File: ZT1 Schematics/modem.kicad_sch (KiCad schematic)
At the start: 3 parts, among them U145 74LS153, U146 74LS153

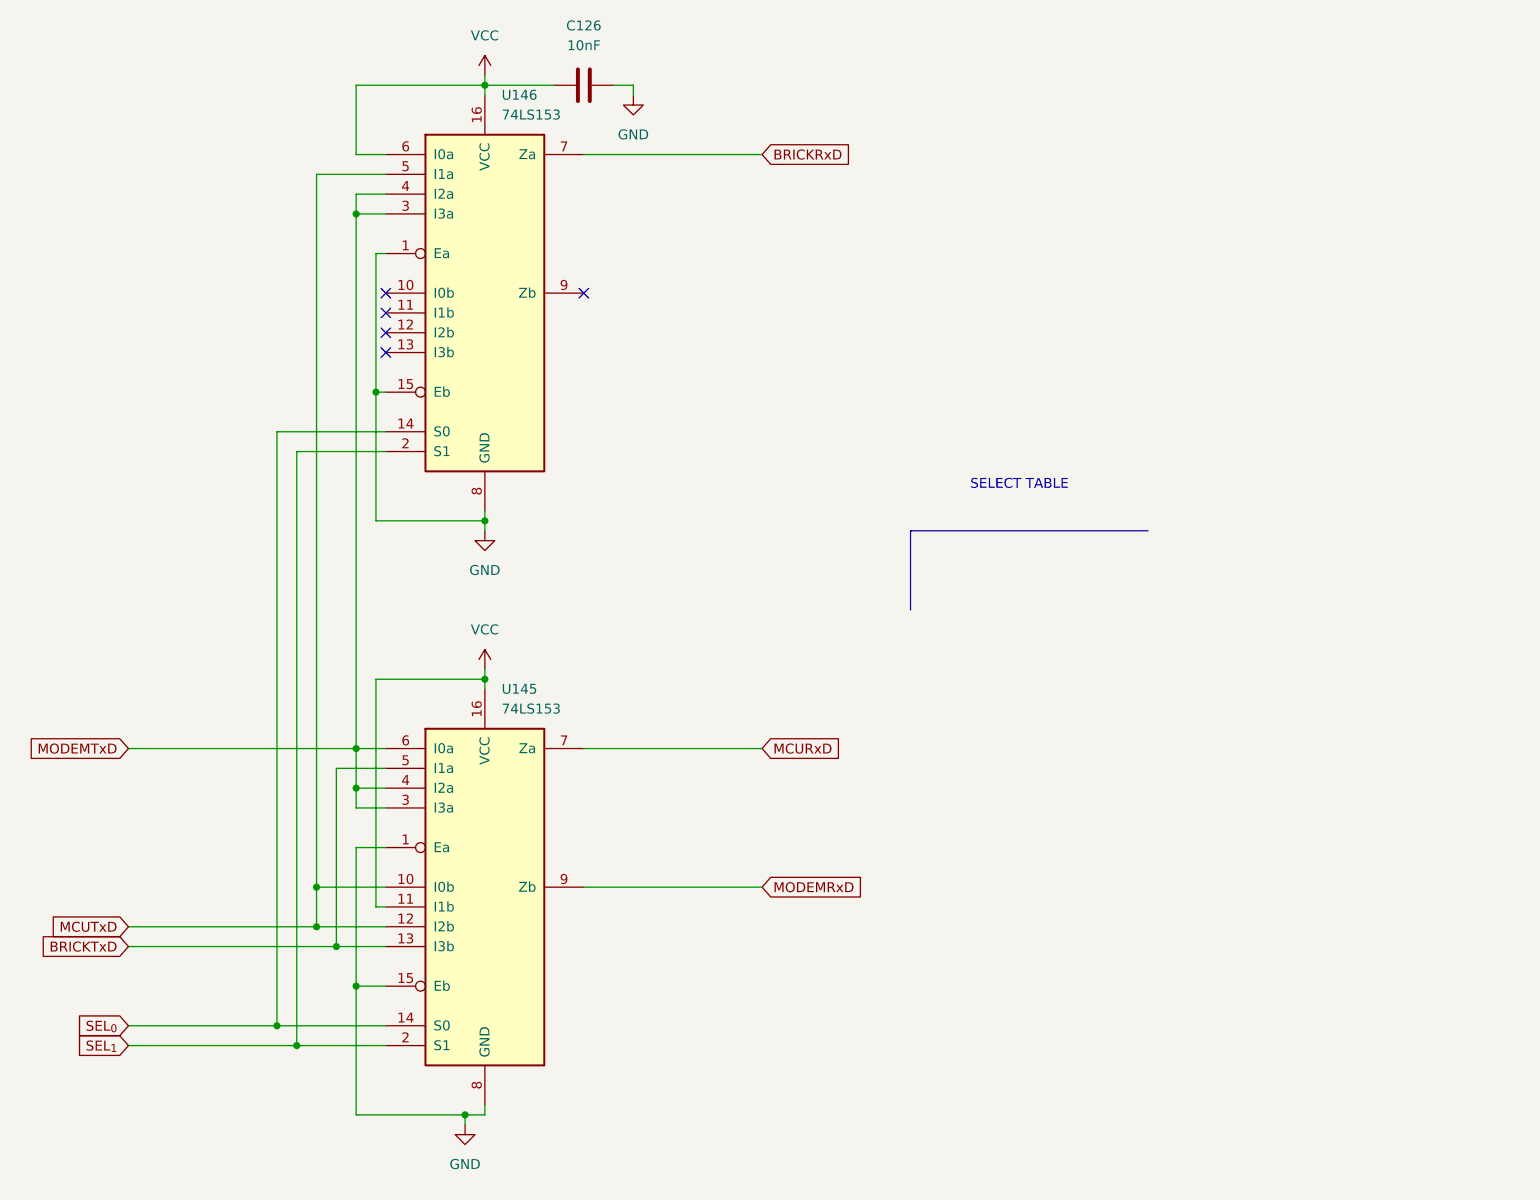
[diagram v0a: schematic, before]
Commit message: Minor touchups
Fixed some of the text
Added some explanations
Simplified the video circuit
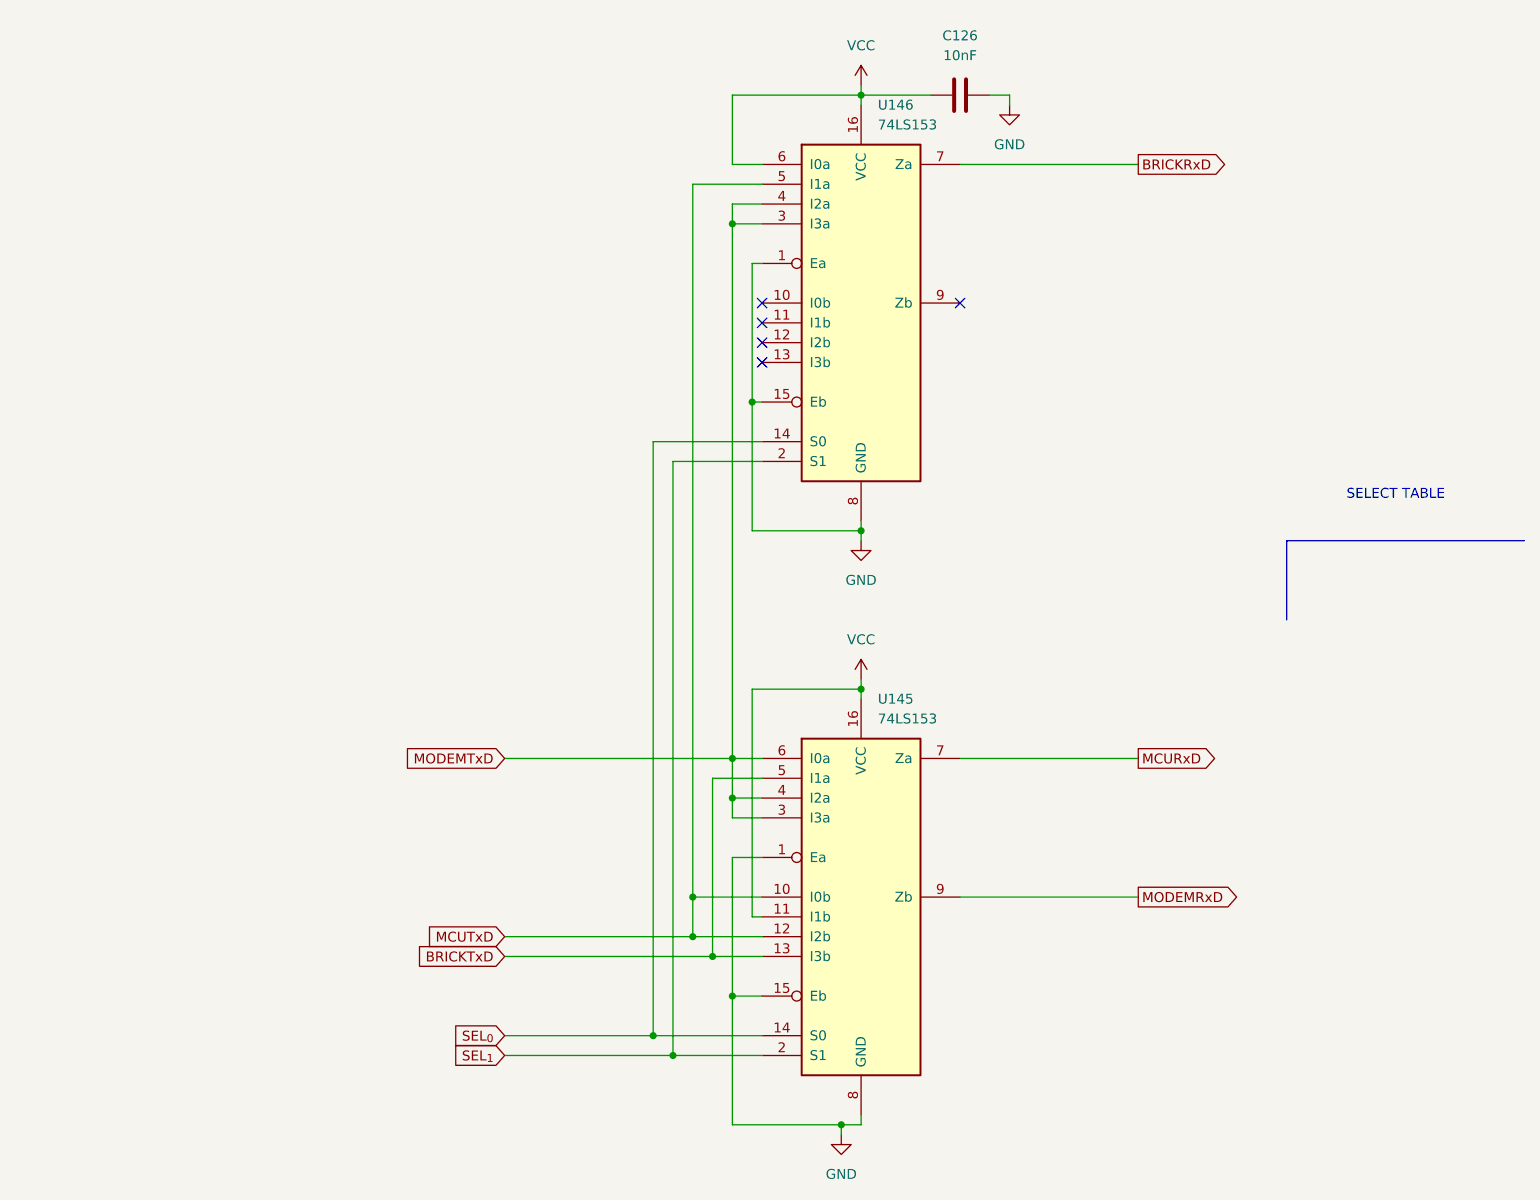
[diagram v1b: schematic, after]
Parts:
- C126: footprint ZX1:C_350mil -> ZT1:C_350mil
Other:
- moved on the sheet: C126, U145, U146
